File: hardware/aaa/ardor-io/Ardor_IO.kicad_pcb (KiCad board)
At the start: 2 copper layers, 100 x 80 mm, 99 parts, among them J101 PI 40-PIN HEADER, J102 CODEC AUX L / GND / R, J202 TO MIDI PANEL / 4,5, J302 TO EXP PANEL / T,R,S, J502 TO YOUR AMP CIRCUIT, J503 TO LINE PANEL / T,S, J602 TO HP PANEL / T,R,S, K501 G5V-1 DC5, Q501 2N7002, U201 H11L1M, U301 ADS1115IDGS, U401 OPA2320AIDR, U402 OPA2320AIDR, U501 OPA2320AIDR, U601 TPA6132A2RTER

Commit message: feat: kicad PCB
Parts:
- H1, H2, H3, H4: footprint MountingHole_3.2mm_M3 -> MountingHole:MountingHole_3.2mm_M3
- moved C502 26.7 mm to (98.0, 98.0), turned to 90 degrees
- moved H4 18.9 mm to (136.0, 110.0)
- moved H3 16.0 mm to (54.0, 110.0)
- moved C301 12.0 mm to (79.0, 96.0)
- moved C302 12.0 mm to (79.0, 99.0)
- moved C303 12.0 mm to (89.0, 97.0)
- moved D301 12.0 mm to (60.0, 93.0)
- moved D302 12.0 mm to (60.0, 101.0)
- moved D303 12.0 mm to (79.0, 92.0)
- moved D304 12.0 mm to (79.0, 103.0)
- moved D305 12.0 mm to (84.0, 91.0)
- moved D306 12.0 mm to (84.0, 103.0)
- moved J302 12.0 mm to (56.0, 95.0)
- moved JP301 12.0 mm to (65.0, 95.0)
- moved R301 12.0 mm to (72.0, 91.0)
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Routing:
- net GND: track 0.00 -> 407.0 mm, vias 0 -> 26
- net CHASSIS: track 0.00 -> 166.6 mm, vias 0 -> 5
- net +5V_PI: track 0.00 -> 90.4 mm, vias 0 -> 1
- net +5V_A: track 0.00 -> 90.0 mm
- net +3V3_ADC: track 0.00 -> 72.4 mm, vias 0 -> 2
- net HP_ENABLE: track 0.00 -> 50.3 mm, vias 0 -> 1
- net /05 / Line and amp feed/AMP_AC: track 0.00 -> 47.4 mm, vias 0 -> 1
- net LINE_ENABLE: track 0.00 -> 42.7 mm, vias 0 -> 1
- net PI_SCL: track 0.00 -> 42.1 mm, vias 0 -> 1
- net BUF_L: track 0.00 -> 41.9 mm, vias 0 -> 2
- net PI_SDA: track 0.00 -> 39.1 mm, vias 0 -> 1
- net AUX_R: track 0.00 -> 38.9 mm
- net /05 / Line and amp feed/AMP_BUF: track 0.00 -> 37.2 mm, vias 0 -> 2
- net EXP_ADC: track 0.00 -> 37.0 mm, vias 0 -> 2
- net AUX_L: track 0.00 -> 34.2 mm
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- added copper zone on B.Cu, net GND
- added copper zone on F.Cu, net GND
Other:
- board size 100 x 80 mm -> 90 x 64 mm
- board text added: "+"
- board text added: "1"
- board text added: "3V3 ADC"
- board text added: "4"
- board text added: "40"
- board text added: "5"
- board text added: "5V A"
- board text added: "AMP"
- board text added: "ARDOR IO"
- board text added: "CODEC AUX"
- board text added: "EXP ADC"
- board text added: "G"
- board text added: "GND"
- board text added: "HP L"
- board text added: "JP301: NORMAL 1-3 / 2-4; REVERSE 3-5 / 4-6"
- board text added: "L"
- board text added: "L G R"
- board text added: "LINE OUT"
- board text added: "MIDI IN"
- board text added: "MIDI RX"
- board text added: "MONO"
- board text added: "PHONES"
- board text added: "POLARITY"
- board text added: "R"
- board text added: "S"
- board text added: "T"
- board text added: "VREF"
- board text removed: "100 x 80 mm / UNROUTED"
- board text removed: "AMP FEED"
- board text removed: "ARDOR IO / PLACEMENT A"
- board text removed: "AUDIO BUFFERS"
- board text removed: "AUX L G R"
- board text removed: "CONTROL ADC"
- board text removed: "HEADPHONES"
- board text removed: "MIDI"
- board text removed: "MIDI ISOLATION CORRIDOR"
- board text removed: "RELAY"

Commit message: feat: smd capacitors
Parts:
- C401, C402, C502, C601, C602: value 2.2u / 63V film -> 2.2u / 16V film; footprint Capacitor_THT:C_Rect_L7.2mm_W7.2mm_P5.00mm_FKS2_FKP2_MKS2_MKP2 -> Ardor_Capacitor:C_Rubycon_MU_3225
- moved C401 2.50 mm to (90.5, 73.0)
- moved C402 2.50 mm to (90.5, 85.0)
- moved C502 2.50 mm to (98.0, 95.5)
- moved C601 2.50 mm to (109.5, 94.0)
- moved C602 2.50 mm to (109.5, 105.0)
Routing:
- net +5V_PI: track 90.4 -> 75.2 mm
- net BUF_R: track 16.9 -> 18.0 mm, vias 1 -> 2
- net BUF_L: track 41.9 -> 43.0 mm, vias 2 -> 3
- net AUX_R: track 38.9 -> 40.0 mm, vias 0 -> 1
- net AUX_L: track 34.2 -> 35.4 mm
- net /06 / Stereo headphones/HP_IN_R: track 11.0 -> 12.2 mm, vias 1 -> 2
- net /06 / Stereo headphones/HP_IN_L: track 12.2 -> 13.3 mm
- net /05 / Line and amp feed/AMP_BUF: track 37.2 -> 38.3 mm
- net /05 / Line and amp feed/AMP_AC: track 47.4 -> 48.6 mm, vias 1 -> 2
- net /04 / Audio distribution/BIAS_R: track 14.4 -> 15.6 mm, vias 1 -> 2
- net /04 / Audio distribution/BIAS_L: track 12.9 -> 14.0 mm
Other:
- board text added: "SIG"
- board text removed: "+"

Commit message: feat: update Ardor IO PCB for hardware rev2
- Refine SMD capacitor routing and placement
- Add capacitor audit and verification artifacts
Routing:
- net +5V_PI: track 75.2 -> 91.4 mm, vias 1 -> 3
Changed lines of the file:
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@@
+	)
+	(segment
+		(start 94 70)
+		(end 100 64)
+		(width 0.4)
+		(layer "F.Cu")
+		(net 4)
 	)
 	(segment
@@
 	)
 	(segment
+		(start 89.225 74.775)
+		(end 90.9 74.775)
+		(width 0.4)
+		(layer "F.Cu")
+		(net 4)
+	)
+	(segment
 		(start 132.7945 84.8555)
 		(end 132 85.65)
@@
 	)
 	(via
+		(at 90.9 74.775)
+		(size 0.6)
+		(drill 0.3)
+		(layers "F.Cu" "B.Cu")
+		(net 4)
+	)
+	(via
 		(at 132.7945 84.8555)
 		(size 0.6)
 		(drill 0.3)
 		(layers "F.Cu" "B.Cu")
+		(net 4)
+	)
+	(via
+		(at 94 70)
+		(size 0.6)
+		(drill 0.3)
+		(layers "F.Cu" "B.Cu")
+		(net 4)
+	)
+	(segment
+		(start 90.9 74.775)
+		(end 94 71.675)
+		(width 0.4)
+		(layer "B.Cu")
 		(net 4)
 	)
@@
 		(layer "B.Cu")
 		(net 4)
+	)
+	(segment
+		(start 94 71.675)
+		(end 94 70)
+		(width 0.4)
+		(layer "B.Cu")
+		(net 4)

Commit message: feat: update Ardor IO PCB for hardware rev2
- Update schematics, routing, BOM, and design documentation
- Add SMD capacitor conversion and verification tooling
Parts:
- C401, C402, C502, C601, C602: value 2.2u / 16V film -> 10u / 50V X7R; footprint Ardor_Capacitor:C_Rubycon_MU_3225 -> Capacitor_SMD:C_1206_3216Metric

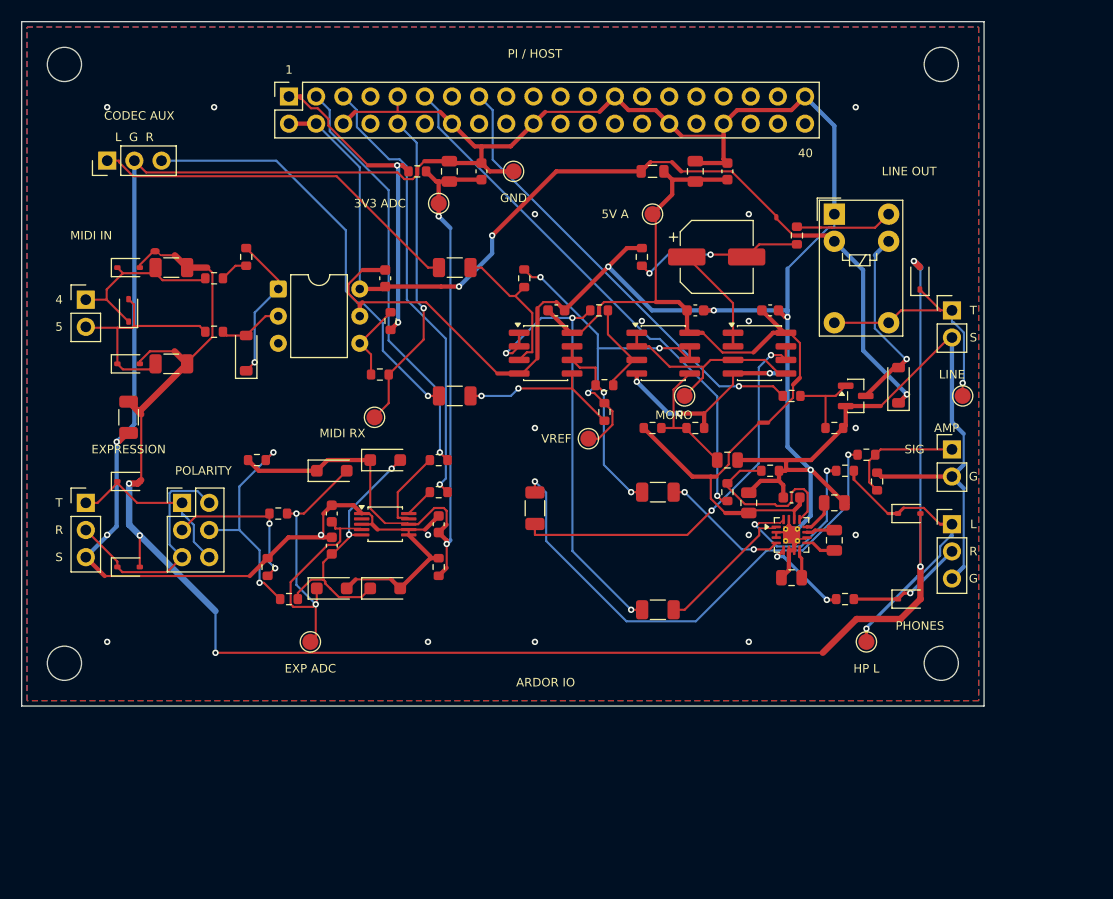
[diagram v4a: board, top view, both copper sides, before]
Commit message: Reduce Ardor IO PCB to 68 x 46 mm and reroute
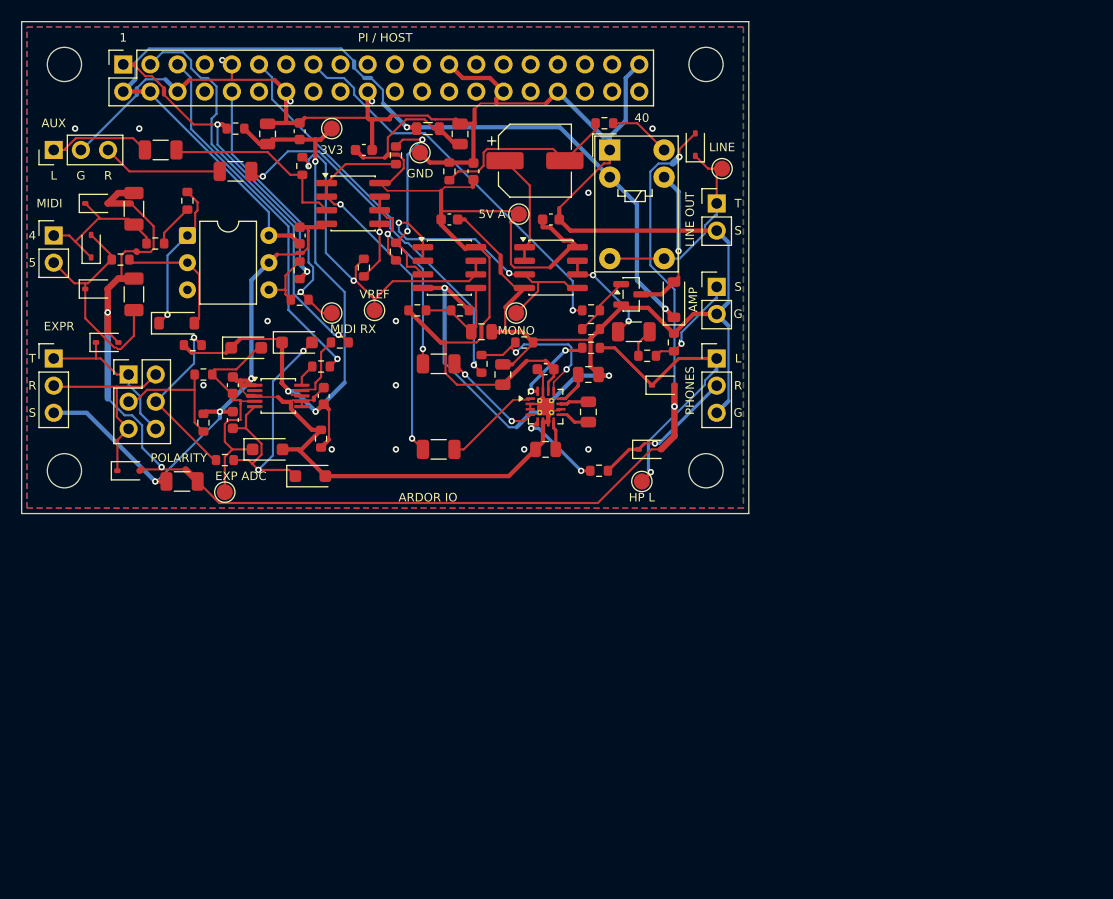
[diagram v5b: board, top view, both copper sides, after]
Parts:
- moved TP501 30.9 mm to (115.5, 63.8)
- moved C401 29.6 mm to (63.0, 62.0)
- moved C402 29.3 mm to (70.0, 64.0)
- moved H4 28.4 mm to (114.0, 92.0)
- moved D602 28.0 mm to (108.8, 90.0)
- moved J602 26.9 mm to (115.0, 81.5)
- moved J502 26.7 mm to (115.0, 74.8)
- moved R603 26.4 mm to (103.2, 80.5)
- moved R402 26.2 mm to (82.0, 73.0)
- moved C403 25.9 mm to (93.0, 79.0)
- moved C603 25.9 mm to (95.0, 83.0)
- moved C604 25.9 mm to (99.0, 82.5)
- moved C605 25.9 mm to (103.0, 83.0)
- moved C606 25.9 mm to (99.0, 90.0)
- moved C607 25.9 mm to (103.0, 86.5)
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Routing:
- net GND: track 407.0 -> 330.3 mm, vias 26 -> 20
- net /05 / Line and amp feed/AMP_AC: track 48.4 -> 2.68 mm, vias 2 -> 0
- net CHASSIS: track 166.6 -> 128.8 mm, vias 5 -> 4
- net AUX_R: track 39.9 -> 11.3 mm, vias 1 -> 0
- net /05 / Line and amp feed/AMP_BUF: track 38.2 -> 9.84 mm
- net AUX_L: track 35.2 -> 9.52 mm
- net EXP_ADC: track 37.0 -> 23.5 mm, vias 2 -> 0
- net HP_ENABLE: track 50.3 -> 37.6 mm
- net +3V3_ADC: track 72.4 -> 62.5 mm, vias 2 -> 3
- net HP_L_RAW: track 17.0 -> 7.43 mm
- net MONO_MIX: track 9.22 -> 17.9 mm, vias 0 -> 2
- net MONO_BUF: track 20.2 -> 28.4 mm, vias 0 -> 2
- net /04 / Audio distribution/BIAS_R: track 15.5 -> 22.9 mm
- net PI_SCL: track 42.1 -> 34.7 mm
- net BUF_L: track 42.9 -> 36.2 mm, vias 3 -> 2
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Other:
- board size 90 x 64 mm -> 68 x 46 mm
- board text added: "3V3"
- board text added: "AUX"
- board text added: "EXPR"
- board text added: "MIDI"
- board text removed: "3V3 ADC"
- board text removed: "CODEC AUX"
- board text removed: "EXPRESSION"
- board text removed: "L G R"
- board text removed: "MIDI IN"
- board text removed: "SIG"

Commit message: feat: finalize Ardor IO hardware rev2 production package
- Update schematics, PCB, BOM, and documentation
- Add assembly exports, review artifacts, and verification data
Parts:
- C102, C104, C201, C301, C302, C303, C404, C405, C503, C604: value 100n / 16V -> 100n / 50V X7R
- C103, C403: value 10u / 10V X7R -> 10u / 16V X7R
- C501: footprint Capacitor_SMD:CP_Elec_6.3x5.4 -> Ardor_Capacitor:CP_Elec_Panasonic_FK_D6.3_H5.8
- C603, C605, C606, C607: value 2.2u / 10V X7R -> 2.2u / 25V X7R
- Q501: value 2N7002 -> AO3400A
